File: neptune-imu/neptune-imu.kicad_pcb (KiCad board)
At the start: 2 copper layers, 0 parts

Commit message: level shifter(bss138) + icm20948 + int lines needed
Also some final things like star(orientattion)
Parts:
- added C1: 100nF, Capacitor_SMD:C_0603_1608Metric, F.Cu at (87.9, 39.0)
- added C10: 100nF, Capacitor_SMD:C_0402_1005Metric, F.Cu at (90.3, 81.1)
- added C14: 1uF, Capacitor_SMD:C_0603_1608Metric, F.Cu at (117.3, 72.6)
- added C15: 1uF, Capacitor_SMD:C_0603_1608Metric, F.Cu at (116.6, 78.3)
- added C2: 100nF, Capacitor_SMD:C_0402_1005Metric, F.Cu at (90.1, 43.3)
- added C22: 4.7uF, Capacitor_SMD:C_0603_1608Metric, F.Cu at (91.4, 43.3)
- added C4: 100nF, Capacitor_SMD:C_0402_1005Metric, F.Cu at (82.8, 48.0)
- added C6: 1uF, Capacitor_SMD:C_0603_1608Metric, F.Cu at (113.1, 72.6)
- added C7: 1uF, Capacitor_SMD:C_0603_1608Metric, F.Cu at (112.7, 78.3)
- added C8: 100nF, Capacitor_SMD:C_0402_1005Metric, F.Cu at (93.5, 81.1)
- added C9: 10uF, Capacitor_SMD:C_0603_1608Metric, F.Cu at (93.5, 82.4)
- added J1: Connector, neptune-imu-footprints:HDR-SMD_8P-P2.00-H-F-W9.2, B.Cu at (99.6, 43.7)
- added J2: Left through connector, neptune-imu-footprints:gaia_connector, F.Cu at (79.4, 59.9)
- added J3: Right through connector, neptune-imu-footprints:gaia_connector, F.Cu at (119.8, 59.9)
- added R1: 10k, Resistor_SMD:R_0402_1005Metric, F.Cu at (81.5, 44.9)
- added SW1: reset, neptune-imu-footprints:KEY-SMD_L4.0-W3.0-LS4.9-1, B.Cu at (87.9, 39.0)
- added TP1: Reset, TestPoint:TestPoint_Pad_1.0x1.0mm, F.Cu at (79.8, 47.9)
- added TP2: boot0, TestPoint:TestPoint_Pad_1.0x1.0mm, F.Cu at (79.8, 45.4)
- added TP3: 3v3, TestPoint:TestPoint_Pad_1.5x1.5mm, F.Cu at (115.7, 40.3)
- added TP4: GND, TestPoint:TestPoint_Pad_1.5x1.5mm, F.Cu at (115.7, 43.9)
- added TP5: Vbus, TestPoint:TestPoint_Pad_1.5x1.5mm, F.Cu at (115.7, 47.4)
- added U1: STM32L432KCUx, neptune-imu-footprints:STM32L432KCUx, F.Cu at (86.5, 45.6)
- added U10: AP2112K-1.8, neptune-imu-footprints:ap2112, F.Cu at (112.5, 75.5)
- added U3: ADXL375BCCZ, neptune-imu-footprints:LGA-14_L5.0-W3.0-P0.80-BL-1, F.Cu at (91.9, 78.5)
- added U5: AP2112K-3.3, neptune-imu-footprints:ap2112, F.Cu at (116.6, 75.5)
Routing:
- net +1V8: track 0.00 -> 42.2 mm, vias 0 -> 3
- net /VOUT_B1: track 0.00 -> 41.3 mm, vias 0 -> 1
- net /reset: track 0.00 -> 22.4 mm, vias 0 -> 1
- net /USART1_TX: track 0.00 -> 20.0 mm, vias 0 -> 1
- net /USART1_RX: track 0.00 -> 18.3 mm, vias 0 -> 1
- net /SWCLK: track 0.00 -> 15.1 mm, vias 0 -> 1
- net GND: track 0.00 -> 13.1 mm, vias 0 -> 17
- net /SWDIO: track 0.00 -> 11.6 mm, vias 0 -> 1
- net /I2C1_SCL: track 0.00 -> 11.5 mm, vias 0 -> 1
- net +3.3V: track 0.00 -> 11.5 mm, vias 0 -> 10
- net /I2C1_SDA: track 0.00 -> 8.24 mm, vias 0 -> 1
- net /boot0: track 0.00 -> 5.28 mm
- net /VOUT_A1: track 0.00 -> 4.17 mm
- net /I2C3_SDA: track 0.00 -> 1.16 mm, vias 0 -> 1
- net /I2C3_SCL: track 0.00 -> 0.92 mm, vias 0 -> 1
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- added copper zone on In2.Cu, net +3.3V
- added copper zone on In1.Cu, net GND
- added copper zone on In4.Cu, net GND
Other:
- board outline added: 50 x 50 mm
- copper layers 2 -> 6
- board text added: "3v3"
- board text added: "Boot0"
- board text added: "GND"
- board text added: "Reset"
- board text added: "Vout"

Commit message: going to school
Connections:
- net /ADXL375/SCL renamed I2C_SCL_1v8
- net /ADXL375/SDA renamed I2C_SDA_1v8
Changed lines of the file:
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@@
 	(net 55 "unconnected-(U1-PA12-Pad22)")
 	(net 56 "unconnected-(U1-PB5-Pad28)")
-	(net 57 "/ADXL375/SCL")
-	(net 58 "/ADXL375/INT2")
-	(net 59 "unconnected-(U3-RESERVED-Pad11)")
-	(net 60 "unconnected-(U3-RESERVED-Pad3)")
-	(net 61 "/ADXL375/SDA")
-	(net 62 "unconnected-(U3-NC-Pad10)")
-	(net 63 "/ADXL375_INT1_1v8")
-	(net 64 "unconnected-(U5-NC-Pad4)")
-	(net 65 "unconnected-(U10-NC-Pad4)")
+	(net 57 "/ADXL375/INT2")
+	(net 58 "unconnected-(U3-RESERVED-Pad11)")
+	(net 59 "unconnected-(U3-RESERVED-Pad3)")
+	(net 60 "unconnected-(U3-NC-Pad10)")
+	(net 61 "/ADXL375_INT1_1v8")
+	(net 62 "unconnected-(U5-NC-Pad4)")
+	(net 63 "unconnected-(U10-NC-Pad4)")
+	(net 64 "I2C_SCL_1v8")
+	(net 65 "I2C_SDA_1v8")
 	(footprint "neptune-imu-footprints:ap2112"
 		(layer "F.Cu")
@@
 			(layers "F.Cu" "F.Mask" "F.Paste")
 			(roundrect_rratio 0.25)
-			(net 65 "unconnected-(U10-NC-Pad4)")
+			(net 63 "unconnected-(U10-NC-Pad4)")
 			(pinfunction "NC")
 			(pintype "no_connect")
@@
 			(layers "F.Cu" "F.Mask" "F.Paste")
 			(roundrect_rratio 0.25)
-			(net 64 "unconnected-(U5-NC-Pad4)")
+			(net 62 "unconnected-(U5-NC-Pad4)")
 			(pinfunction "NC")
 			(pintype "no_connect")
@@
 			(size 0.55 1.3)
 			(layers "F.Cu" "F.Mask" "F.Paste")
-			(net 60 "unconnected-(U3-RESERVED-Pad3)")
+			(net 59 "unconnected-(U3-RESERVED-Pad3)")
 			(pinfunction "RESERVED")
 			(pintype "unspecified+no_connect")
@@
 			(size 0.55 1.3)
 			(layers "F.Cu" "F.Mask" "F.Paste")
-			(net 63 "/ADXL375_INT1_1v8")
+			(net 61 "/ADXL375_INT1_1v8")
 			(pinfunction "INT1")
 			(pintype "unspecified")
@@
 			(size 0.55 1.3)
 			(layers "F.Cu" "F.Mask" "F.Paste")
-			(net 58 "/ADXL375/INT2")
+			(net 57 "/ADXL375/INT2")
 			(pinfunction "INT2")
 			(pintype "unspecified+no_connect")
@@
 			(size 0.55 1.3)
 			(layers "F.Cu" "F.Mask" "F.Paste")
-			(net 62 "unconnected-(U3-NC-Pad10)")
+			(net 60 "unconnected-(U3-NC-Pad10)")
 			(pinfunction "NC")
 			(pintype "unspecified+no_connect")
@@
 			(size 0.55 1.3)
 			(layers "F.Cu" "F.Mask" "F.Paste")
-			(net 59 "unconnected-(U3-RESERVED-Pad11)")
+			(net 58 "unconnected-(U3-RESERVED-Pad11)")
 			(pinfunction "RESERVED")
 			(pintype "unspecified+no_connect")
@@
 			(size 0.55 1.3)
 			(layers "F.Cu" "F.Mask" "F.Paste")
-			(net 61 "/ADXL375/SDA")
+			(net 65 "I2C_SDA_1v8")
 			(pinfunction "SDA/SDI/SDIO")
 			(pintype "unspecified")
@@
 			(size 1.3 0.6)
 			(layers "F.Cu" "F.Mask" "F.Paste")
-			(net 57 "/ADXL375/SCL")
+			(net 64 "I2C_SCL_1v8")
 			(pinfunction "SCL/SCLK")
 			(pintype "unspecified")
@@
 	)
 	(via
-		(at 89.7115 78.4825)
+		(at 93.9415 77.2625)
 		(size 0.5)
 		(drill 0.3)
 		(layers "F.Cu" "B.Cu")
-		(net 57)
+		(net 61)
 	)
 	(via
-		(at 89.9415 77.2625)
+		(at 89.7115 78.4825)
 		(size 0.5)
 		(drill 0.3)
 		(layers "F.Cu" "B.Cu")
-		(net 61)
+		(net 64)
 	)
 	(via
-		(at 93.9415 77.2625)
+		(at 89.9415 77.2625)
 		(size 0.5)
 		(drill 0.3)
 		(layers "F.Cu" "B.Cu")
-		(net 63)
+		(net 65)
 	)
 	(zone

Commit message: final
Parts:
- added C11: 100nF, Capacitor_SMD:C_0402_1005Metric, F.Cu at (103.0, 82.2)
- added C3: 100nF, Capacitor_SMD:C_0402_1005Metric, F.Cu at (105.6, 78.6)
- added C5: 100nF, Capacitor_SMD:C_0402_1005Metric, F.Cu at (102.3, 81.2)
- added Q1: BSS138, neptune-imu-footprints:bss138, F.Cu at (96.8, 76.0)
- added Q2: BSS138, neptune-imu-footprints:bss138, F.Cu at (96.8, 79.8)
- added R2: 10k, Resistor_SMD:R_0402_1005Metric, F.Cu at (99.3, 76.0)
- added R3: 10k, Resistor_SMD:R_0402_1005Metric, F.Cu at (94.2, 76.5)
- added R4: 10k, Resistor_SMD:R_0402_1005Metric, F.Cu at (99.3, 79.8)
- added R5: 10k, Resistor_SMD:R_0402_1005Metric, F.Cu at (94.2, 80.3)
- added R6: 10k, Resistor_SMD:R_0402_1005Metric, F.Cu at (88.7, 49.5)
- added R7: 0, Resistor_SMD:R_0402_1005Metric, F.Cu at (106.2, 80.4)
- added U2: ICM20948, neptune-imu-footprints:icm20948, F.Cu at (103.0, 78.6)
- moved U3 3.41 mm to (88.5, 78.5)
- moved C10 3.41 mm to (86.9, 81.2)
- moved C8 3.41 mm to (90.1, 81.2)
- moved C9 3.41 mm to (90.1, 82.4)
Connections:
- J2 pad 1: unconnected-(J2-Pin_1-Pad1) -> /I2C_2_SDA
- J2 pad 2: /I2C1_SDA -> unconnected-(J2-Pin_2-Pad2)
- J2 pad 3: unconnected-(J2-Pin_3-Pad3) -> /I2C_2_SCL
- J2 pad 4: /I2C1_SCL -> unconnected-(J2-Pin_4-Pad4)
- U1 pad 29: /I2C1_SCL -> /I2C_2_SCL
- U1 pad 30: /I2C1_SDA -> /I2C_2_SDA
- U1 pad 7: unconnected-(U1-PA1-Pad7) -> /ADXL375_INT1_1v8
- U1 pad 8: unconnected-(U1-PA2-Pad8) -> /ICM209481_INT_1v8
- U3 pad 13: I2C_SDA_1v8 -> /I2C3_SDA
- U3 pad 14: I2C_SCL_1v8 -> /I2C3_SCL
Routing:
- net /ICM209481_INT_1v8: track 0.00 -> 49.1 mm
- net /I2C3_SCL: track 0.92 -> 49.6 mm, vias 1 -> 3
- net /I2C3_SDA: track 1.16 -> 46.6 mm, vias 1 -> 3
- net /ADXL375_INT1_1v8: track 0.00 -> 33.4 mm, vias 1 -> 0
- net +1V8: track 42.2 -> 67.4 mm, vias 3 -> 4
- net /I2C_2_SCL: track 0.00 -> 14.4 mm, vias 0 -> 1
- net /I2C1_SCL: track 11.5 -> 0.00 mm, vias 1 -> 0
- net /I2C_2_SDA: track 0.00 -> 8.57 mm, vias 0 -> 1
- net /I2C1_SDA: track 8.24 -> 0.00 mm, vias 1 -> 0
- net /VOUT_B1: track 41.3 -> 48.9 mm, vias 1 -> 0
- net I2C_SCL_1v8: track 0.00 -> 5.87 mm, vias 1 -> 0
- net I2C_SDA_1v8: track 0.00 -> 5.68 mm, vias 1 -> 0
- net GND: track 13.1 -> 17.3 mm, vias 17 -> 38
- net Net-(U2-REGOUT): track 0.00 -> 2.16 mm
- net /ICM20948 sensors/1_INT: track 0.00 -> 1.74 mm
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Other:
- board text added: "Inertial Measurement Unit"
- board text added: "revision 1.0 Project Neptune"

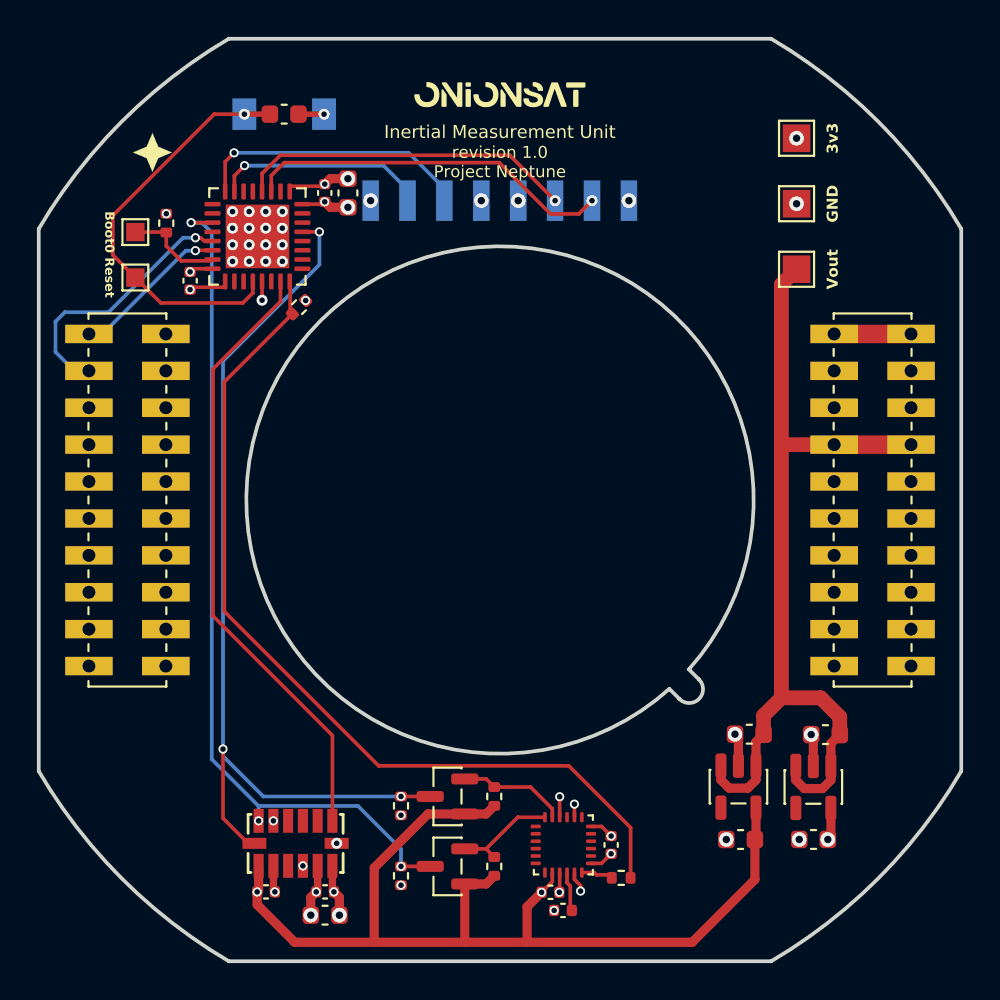
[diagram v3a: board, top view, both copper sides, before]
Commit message: icm20948 updated for bss138 level shifting
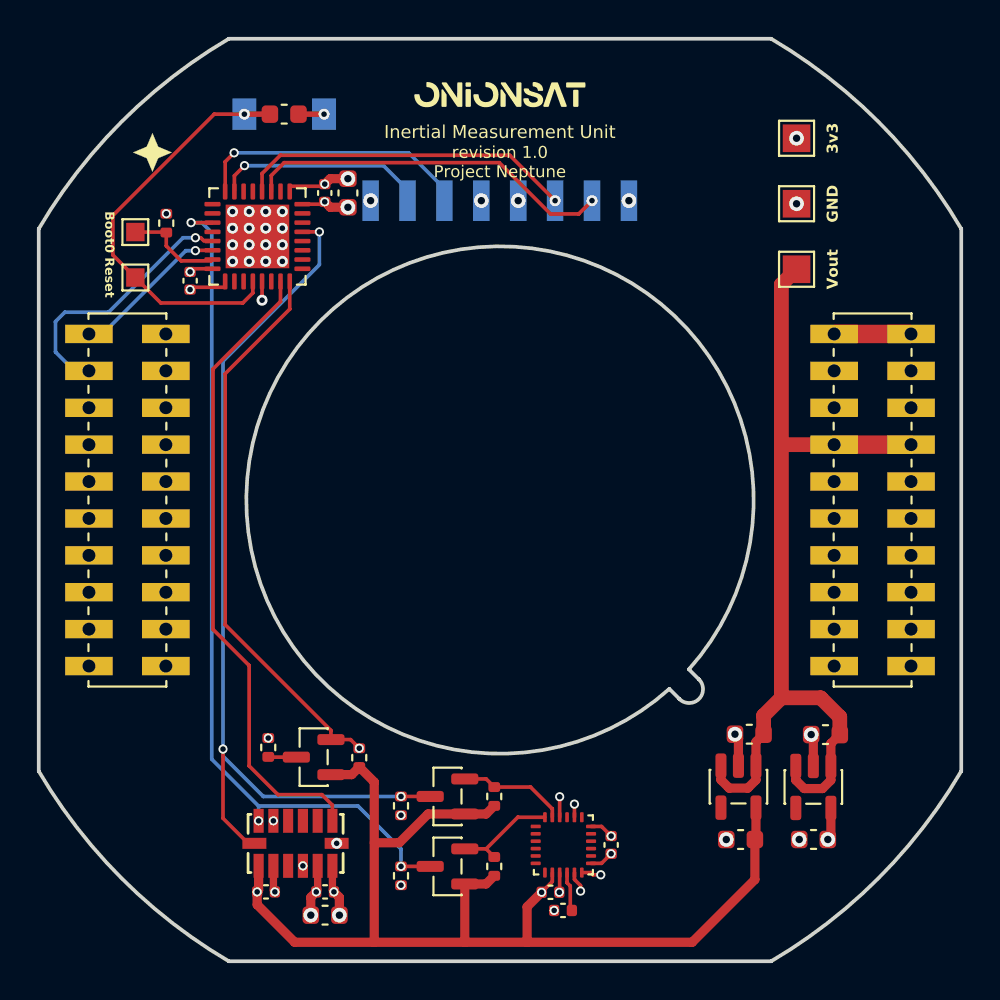
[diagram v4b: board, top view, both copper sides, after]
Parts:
- removed R6: 10k, Resistor_SMD:R_0402_1005Metric
- removed R7: 0, Resistor_SMD:R_0402_1005Metric
- added Q3: BSS138, neptune-imu-footprints:bss138, F.Cu at (89.5, 73.9)
- added R8: 10k, Resistor_SMD:R_0402_1005Metric, F.Cu at (92.0, 73.9)
- added R9: 10k, Resistor_SMD:R_0402_1005Metric, F.Cu at (87.1, 73.3)
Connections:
- net /ADXL375_INT1_1v8 renamed /ADXL375_INT1_3v3
- U2 pad 12: /ICM20948 sensors/1_INT -> /ICM209481_INT_1v8
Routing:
- net +1V8: track 67.4 -> 74.4 mm
- net /ICM20948 sensors/1_INT: track 1.74 -> 0.00 mm
- net /ICM209481_INT_3v3: track 0.00 -> 1.53 mm
- net /ADXL375_INT1_3v3: track 33.4 -> 34.8 mm
- net /ICM209481_INT_1v8: track 49.1 -> 49.5 mm, vias 0 -> 2

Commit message: fixing bugs, production
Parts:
- moved TP3 2.59 mm to (113.3, 39.4)
- moved TP4 2.59 mm to (113.3, 43.0)
- moved TP5 2.59 mm to (113.3, 46.5)
- moved C1 0.89 mm to (88.0, 38.1)
- moved SW1 0.69 mm to (88.0, 38.3)
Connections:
- C10 pad 2: +1V8 -> +3.3V
- J2 pad 10: unconnected-(J2-Pin_10-Pad10) -> GND
- U1 pad 8: /ICM209481_INT_1v8 -> /ICM209481_INT_3v3
- U3 pad 1: +1V8 -> +3.3V
- U3 pad 12: +1V8 -> GND
- U3 pad 7: GND -> +3.3V
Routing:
- net /ICM209481_INT_3v3: track 1.53 -> 30.6 mm
- net /ICM209481_INT_1v8: track 49.5 -> 20.9 mm
- net +1V8: track 74.4 -> 59.3 mm, vias 4 -> 2
- net /VOUT_B1: track 48.9 -> 50.1 mm
- net GND: track 17.3 -> 16.2 mm
- net /I2C_2_SCL: track 14.4 -> 13.5 mm
- net /I2C_2_SDA: track 8.57 -> 7.83 mm
- net /SWCLK: track 15.1 -> 14.5 mm
- net /SWDIO: track 11.6 -> 11.0 mm
- net +3.3V: vias 14 -> 16
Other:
- board text added: "3V3"
- board text added: "B0"
- board text added: "RESET"
- board text added: "RST"
- board text added: "VIN"
- board text removed: "3v3"
- board text removed: "Boot0"
- board text removed: "Reset"
- board text removed: "Vout"
